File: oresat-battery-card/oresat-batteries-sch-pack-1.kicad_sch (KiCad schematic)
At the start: 92 parts, among them Q10 SI7111EDN-T1-GE3, Q13 SI7111EDN-T1-GE3, Q14 DMP2035UQ-7, Q15 DMP2035UQ-7, Q16 SI7111EDN-T1-GE3, Q17 SI7111EDN-T1-GE3, Q18 SI7111EDN-T1-GE3, Q19 SI7111EDN-T1-GE3, Q23 DMP2035UQ-7, Q29 SQS484ENW-T1_GE3, Q6 DMN2053UQ-13, Q7 DMN2053UQ-13, Q8 DMN2053UQ-13, Q9 DMN2053UQ-13, U10 TPS25983, U11 LTC4412, U12 MAX17205G, U8 S-8209AAA-T8T1U, U9 S-8209AAA-T8T1U

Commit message: Jumped back on the TPS bandwagon - LCSC to the rescue! - and lots of cleanup.
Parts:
- removed Q10: SI7111EDN-T1-GE3, Package_SO:Vishay_PowerPAK_1212-8_Single, symbol Transistor_FET:SiS443DN
- removed R69: 100k, oresat-passives:0603-C-NOSILK, symbol Device:R_Small_US
- added TP37, TP47: TEST-POINT-LARGE-SQUARE, oresat-misc:TestPoint-0.75mm-th, symbol oresat-misc:Test-Point-0.75mm-th
- C19: DPN 399-6856-1-ND -> (none); MPN C0603C104K5RACAUTO -> (none)
- JP1, JP2: now not fitted
- R107: value 100k -> 357K; DPN RMCF0603FT100KCT-ND -> RMCF0603FT357KCT-ND; MPN RMCF0603FT100K -> RMCF0603FT357K
- R45, R48, R52, R53: DPN RMCF0603FT2K70CT-ND -> RMCF0603FT1K00CT-ND
- R68: value 100k -> 2; DPN RMCF0603FT100KCT-ND -> RMCF0603FT2R00DKR-ND; MPN RMCF0603FT100K -> RMCF0603FT2R00
- R72: value 1870 -> 1k; DPN RMCF0603FT100KCT-ND -> RMCF0603FT1K00CT-ND; MPN RMCF0603FT100K -> RMCF0603FT1K00
- R74: value 210 -> 154; DPN RMCF0603FT100KCT-ND -> 738-RMCF0603FT154RCT-ND; MPN RMCF0603FT100K -> RMCF0603FT154R
- U10: value TPS25983 -> TPS259830ONRGER; DPN 296-TPS259830LNRGERCT-ND -> 296-TPS259830ONRGERCT-ND; MPN TPS25983 -> TPS259830ONRGER
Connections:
- net POS-BATT-DISC: now also R104.2, R107.1, U10.6 (EN/UVLO), TP47.1
- net VBUS: now also C10.1, C23.1, Q13.1 (S), Q13.2 (S), Q13.3 (S), Q18.5 (D), TP36.1, U11.1 (VIN)
- net at R72.1, U10.9 (IMON): now also TP37.1
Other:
- note added: "EFUSE Current limit: 8.0 A (circuit breaker set to +20%, 9.6 A) Voltage ramp up time: 24 ms Transient overcurrent timer: 2.0 ms Time between retries: 4.6 s"
- note added: "Q29 disconnects the - battery lead, but it also kills the ground reference for the ~{SHUTDOOWN} circuit, which is bad because it turns on the ABLIC and MAX17 chips. So, R93 preserves the ground reference while not allowing any appreciable current to flow."
- note removed: "EFUSE Current limit: 7.1 A Voltage ramp up time: 24 ms Transient overcurrent timer: 2.0 ms Time between retries: 4.6 s"
- note removed: "Q29 disconnects the - battery lead, but it also kills the ground reference for the ~{SHUTDOOWN} circuit, which is bad because it turns on the ABLIC and MAX17 chips. So, R93 preserves the ground reference while not allow anny appreciable current to flow."
- moved on the sheet: C10, Q29, R62, R85, R93, TP42, TP43

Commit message: Battery Card 4.0, no ERC or DRC errors or warnings
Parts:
- R107: value 357K -> 357k
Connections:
- net BATTNEG-PK1: no longer B2.2 (-), Q29.1 (S), Q29.2 (S), Q29.3 (S), R93.2, TP42.1
- new net: B2.2 (-), Q29.1 (S), Q29.2 (S), Q29.3 (S), R93.2, TP42.1
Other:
- note added: "TVS diode is next to main connector"
- moved on the sheet: C20, C21, C24, C25, D5, D6, JP1, JP2, Q14, Q15, Q16, Q17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

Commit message: Updated Makefile and Readme; fixed TCAN IC, cleanup, fix battery connections that were killed somehow
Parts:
- C19: DPN (none) -> 399-12984-1-ND; MPN (none) -> C0603C153K5RACAUTO
- R62: DPN 696-1374-1-ND -> WSLP-.01CT-ND; MFR Riedon -> Vishay Dale; MPN CSR1206-0R01F1 -> WSLP1206R0100FEA
- R68: DPN RMCF0603FT2R00DKR-ND -> RMCF0603FT2R00CT-ND
- U11: DPN MAX4211FETE+-ND -> LTC4412ES6#WTRMPBF; MPN MAX4211FETE -> LTC4412ES6#PBF
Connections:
- net BATTNEG-PK1: now also B2.2 (-), Q29.1 (S), Q29.2 (S), Q29.3 (S), R93.2, TP42.1
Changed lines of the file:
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@@
 	)
 	(junction
-		(at 365.76 294.64)
-		(diameter 0)
-		(color 0 0 0 0)
-	)
-	(junction
 		(at 365.76 270.51)
 		(diameter 0)
@@
 	)
 	(junction
+		(at 374.65 294.64)
+		(diameter 0)
+		(color 0 0 0 0)
+	)
+	(junction
 		(at 171.45 273.05)
 		(diameter 0)
@@
 	)
 	(junction
+		(at 365.76 294.64)
+		(diameter 0)
+		(color 0 0 0 0)
+	)
+	(junction
 		(at 327.66 82.55)
 		(diameter 0)
@@
 	)
 	(junction
+		(at 374.65 295.91)
+		(diameter 0)
+		(color 0 0 0 0)
+	)
+	(junction
 		(at 353.06 200.66)
 		(diameter 0)
@@
 	(wire
 		(pts
+			(xy 374.65 295.91) (xy 374.65 298.45)
+		)
+		(stroke
+			(width 0.381)
+			(type default)
+		)
+	)
+	(wire
+		(pts
 			(xy 231.14 163.83) (xy 231.14 172.72)
 		)
@@
 	(wire
 		(pts
-			(xy 365.76 294.64) (xy 422.91 294.64)
-		)
-		(stroke
-			(width 0.1524)
-			(type solid)
-		)
-	)
-	(wire
-		(pts
 			(xy 474.98 195.58) (xy 474.98 194.31)
 		)
@@
 	(wire
 		(pts
-			(xy 374.65 290.83) (xy 374.65 298.45)
+			(xy 374.65 290.83) (xy 374.65 294.64)
 		)
 		(stroke
@@
 	(wire
 		(pts
-			(xy 422.91 243.84) (xy 422.91 294.64)
+			(xy 422.91 243.84) (xy 422.91 295.91)
 		)
 		(stroke
@@
 	(wire
 		(pts
+			(xy 374.65 295.91) (xy 422.91 295.91)
+		)
+		(stroke
+			(width 0.1524)
+			(type solid)
+		)
+	)
+	(wire
+		(pts
 			(xy 485.14 195.58) (xy 485.14 194.31)
 		)
@@
 	(wire
 		(pts
+			(xy 365.76 294.64) (xy 374.65 294.64)
+		)
+		(stroke
+			(width 0.1524)
+			(type solid)
+		)
+	)
+	(wire
+		(pts
 			(xy 170.18 264.16) (xy 179.07 264.16)
 		)
@@
 	(wire
 		(pts
+			(xy 374.65 294.64) (xy 374.65 295.91)
+		)
+		(stroke
+			(width 0.381)
+			(type default)
+		)
+	)
+	(wire
+		(pts
 			(xy 374.65 71.12) (xy 374.65 72.39)
 		)
@@
 			)
 		)
-		(property "Datasheet" "https://search.kemet.com/download/specsheet/C0603C104K5RACAUTO"
+		(property "Datasheet" "https://yageogroup.com/content/datasheet/asset/file/KEM_C1023_X7R_AUTO_SMD"
 			(at 322.58 86.36 0)
 			(hide yes)
@@
 			)
 		)
-		(property "Description" ""
+		(property "Description" "0.015 µF ±10% 50V Ceramic Capacitor X7R 0603 (1608 Metric)"
 			(at 322.58 86.36 0)
 			(hide yes)
@@
 			)
 		)
-		(property "DPN" ""
+		(property "DPN" "399-12984-1-ND"
 			(at 322.58 86.36 0)
 			(hide yes)
@@
 			)
 		)
-		(property "MPN" ""
+		(property "MPN" "C0603C153K5RACAUTO"
 			(at 322.58 86.36 0)
 			(hide yes)
@@
 		)
 		(property "Value" "10n"
-			(at 249.174 188.976 0)
+			(at 249.174 188.468 0)
 			(show_name no)
 			(do_not_autoplace no)
@@
 			)
 		)
-		(property "DPN" "RMCF0603FT2R00DKR-ND"
+		(property "DPN" "RMCF0603FT2R00CT-ND"
 			(at 334.01 82.55 0)
 			(hide yes)
@@
 			)
 		)
-		(property "Datasheet" "https://www.mouser.com/datasheet/2/256/MAX4210-MAX4211-1265251.pdf"
+		(property "Datasheet" "https://www.analog.com/media/en/technical-documentation/data-sheets/ltc4412.pdf"
 			(at 377.19 99.06 0)
 			(hide yes)
@@
 			)
 		)
-		(property "Description" "Current Monitor Regulator High-Side 16-TQFN (4x4)"
+		(property "Description" "OR Controller Source Selector Switch P-Channel 2:1 TSOT-23-6 industrial temp"
 			(at 430.53 93.98 0)
 			(hide yes)
@@
 			)
 		)
-		(property "DPN" "MAX4211FETE+-ND"
+		(property "DPN" "LTC4412ES6#WTRMPBF"
 			(at 430.53 93.98 0)
 			(hide yes)
@@
 			)
 		)
-		(property "MPN" "MAX4211FETE"
+		(property "MPN" "LTC4412ES6#PBF"
 			(at 430.53 93.98 0)
 			(hide yes)
@@
 			)
 		)
-		(property "Datasheet" "https://riedon.com/media/pdf/CSR.pdf"
+		(property "Datasheet" "https://www.vishay.com/docs/30122/wslp.pdf"
 			(at 374.65 323.85 0)
 			(hide yes)
@@
 			)
 		)
-		(property "Description" "10 mOhms ±1% 1W Chip Resistor 1206 (3216 Metric) Current Sense, Non-Inductive Metal Element"
+		(property "Description" "10 mOhms ±1% 1W Chip Resistor 1206 (3216 Metric) Anti-Sulfur, Automotive AEC-Q200, Current Sense, Moisture Resistant, Pulse Withstanding Metal Element"
 			(at 374.65 323.85 0)
 			(hide yes)
@@
 			)
 		)
-		(property "DPN" "696-1374-1-ND"
+		(property "DPN" "WSLP-.01CT-ND"
 			(at 374.65 323.85 0)
 			(hide yes)
@@
 			)
 		)
-		(property "MFR" "Riedon"
+		(property "MFR" "Vishay Dale"
 			(at 374.65 323.85 0)
 			(hide yes)
@@
 			)
 		)
-		(property "MPN" "CSR1206-0R01F1"
+		(property "MPN" "WSLP1206R0100FEA"
 			(at 374.65 323.85 0)
 			(hide yes)
@@
 		(lib_id "Device:C_Small")
 		(at 231.14 175.26 0)
+		(mirror y)
 		(unit 1)
 		(body_style 1)
@@
 		(dnp no)
 		(property "Reference" "C17"
-			(at 233.426 174.752 0)
+			(at 228.854 174.752 0)
 			(show_name no)
 			(do_not_autoplace no)
@@
 		)
 		(property "Value" "100n"
-			(at 233.68 176.784 0)
+			(at 228.6 176.784 0)
 			(show_name no)
 			(do_not_autoplace no)

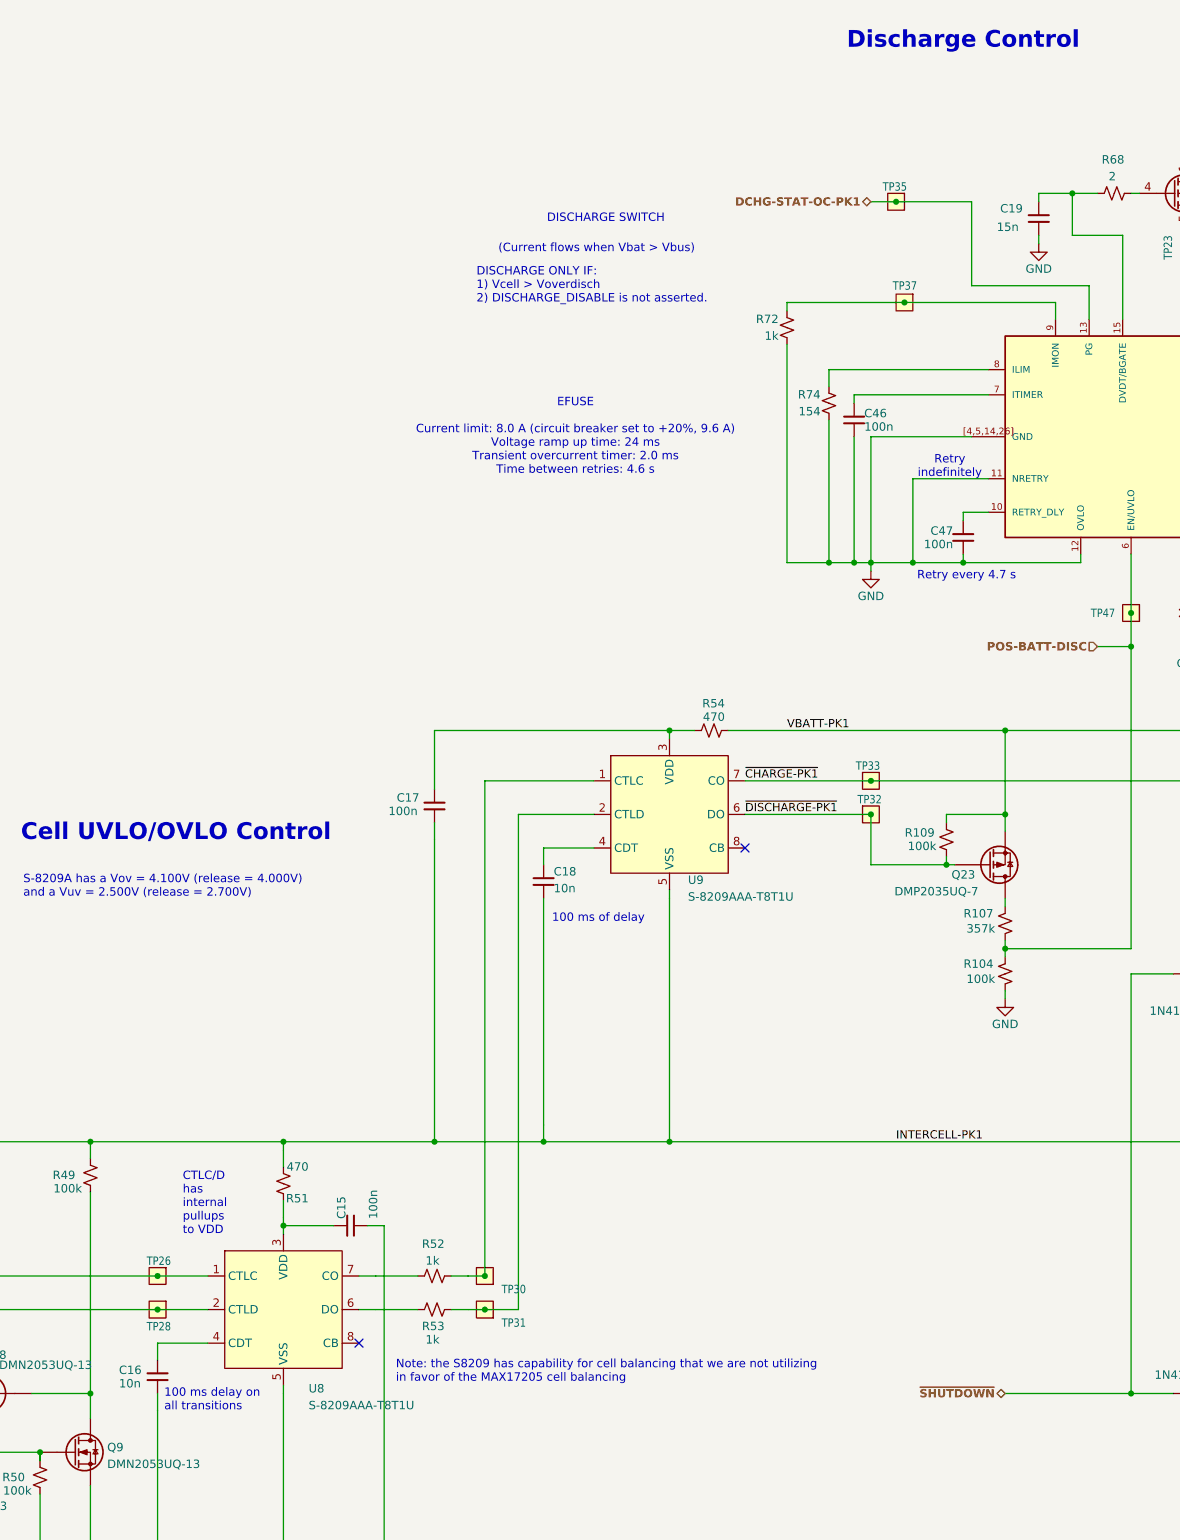
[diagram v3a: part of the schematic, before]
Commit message: Changes to eFuse after trying evaluation board, and recalculating values, and trying to reduce number of passive components to minimum number
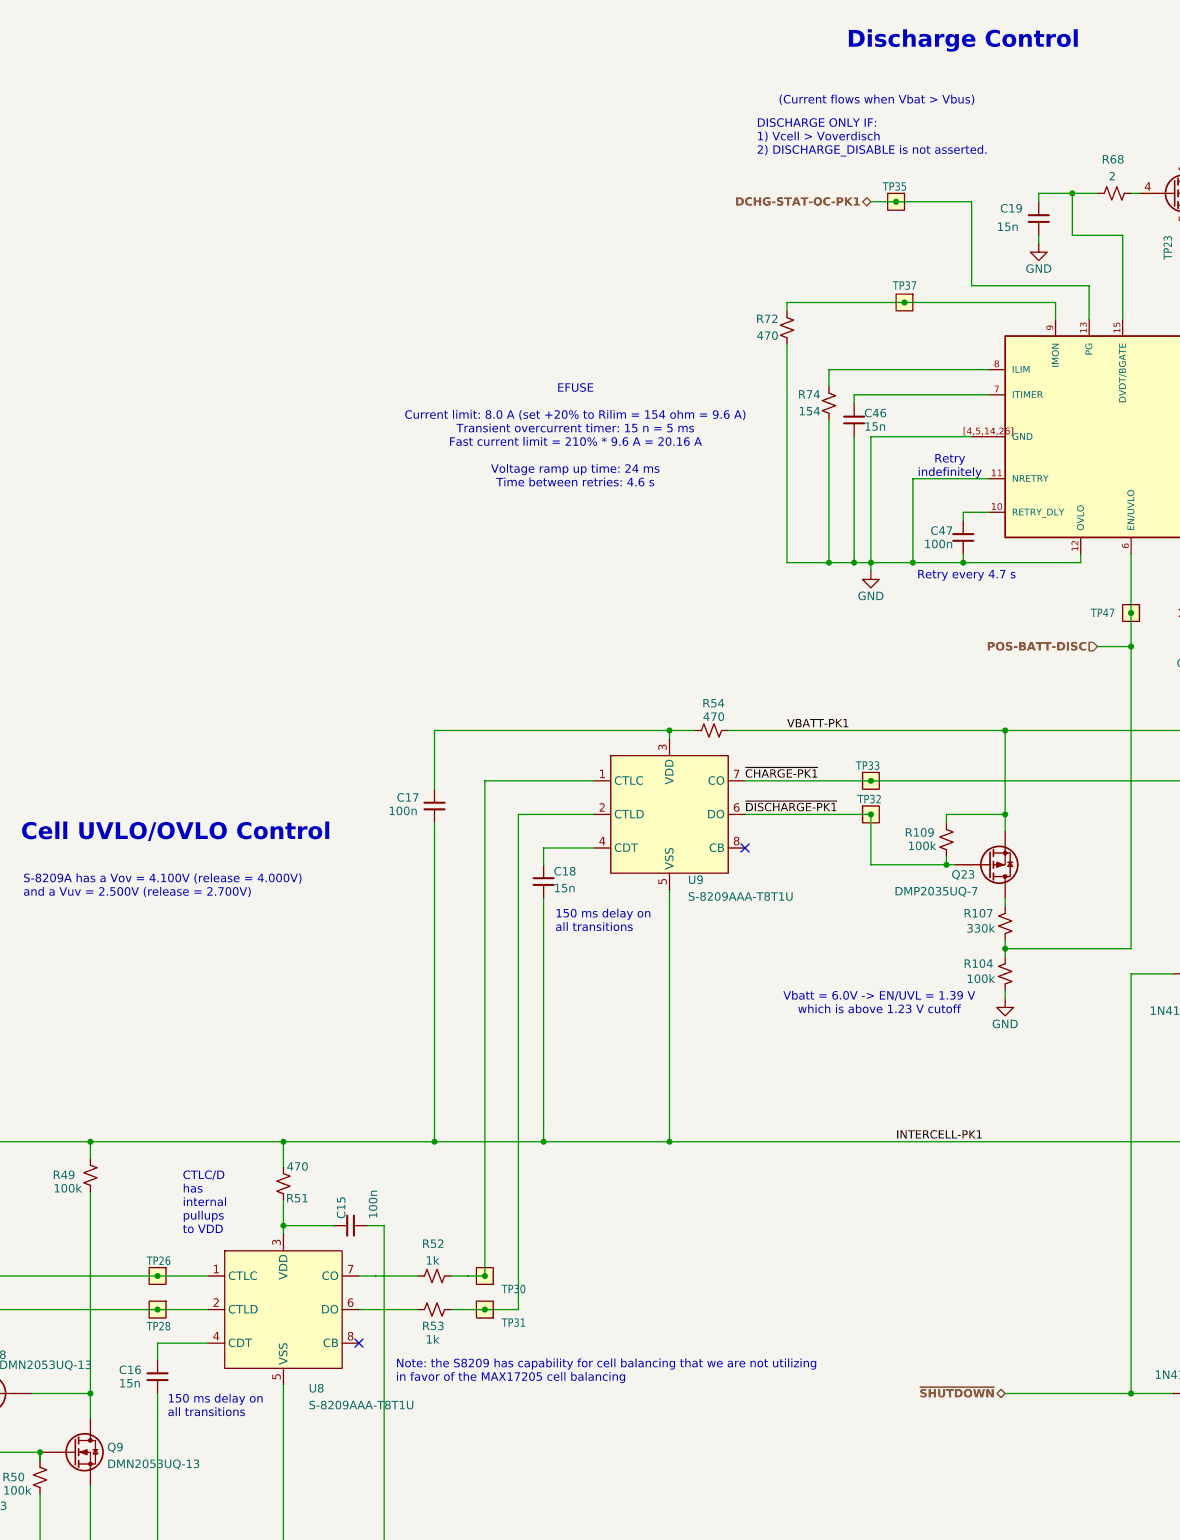
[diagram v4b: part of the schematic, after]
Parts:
- C16, C18: value 10n -> 15n; DPN 399-12983-1-ND -> 399-12984-1-ND; MPN C0603C103J5RACAUTO -> C0603C153K5RACAUTO
- C46: value 100n -> 15n; DPN 399-6856-1-ND -> 399-12984-1-ND; MPN C0603C104K5RACAUTO -> C0603C153K5RACAUTO
- R107: value 357k -> 330k; DPN RMCF0603FT357KCT-ND -> RMCF0603FT330KCT-ND; MPN RMCF0603FT357K -> RMCF0603FT330K
- R72: value 1k -> 470; DPN RMCF0603FT1K00CT-ND -> RMCF0603FT470RCT-ND; MPN RMCF0603FT1K00 -> RMCF0603FT470R
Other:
- note added: "150 ms delay on all transitions"
- note added: "EFUSE Current limit: 8.0 A (set +20% to Rilim = 154 ohm = 9.6 A) Transient overcurrent timer: 15 n = 5 ms Fast current limit = 210% * 9.6 A = 20.16 A Voltage ramp up time: 24 ms Time between retries: 4.6 s"
- note added: "Vbatt = 6.0V -> EN/UVL = 1.39 V which is above 1.23 V cutoff"
- note removed: "100 ms delay on all transitions"
- note removed: "100 ms of delay"
- note removed: "DISCHARGE SWITCH"
- note removed: "EFUSE Current limit: 8.0 A (circuit breaker set to +20%, 9.6 A) Voltage ramp up time: 24 ms Transient overcurrent timer: 2.0 ms Time between retries: 4.6 s"
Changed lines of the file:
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@@
 		)
 	)
+	(text "150 ms delay on\nall transitions"
+		(exclude_from_sim no)
+		(at 190.754 267.97 0)
+		(effects
+			(font
+				(size 1.27 1.27)
+			)
+			(justify left bottom)
+		)
+	)
 	(text "CTLC/D\nhas\ninternal\npullups\nto VDD"
 		(exclude_from_sim no)
@@
 		)
 	)
-	(text "EFUSE\n\nCurrent limit: 8.0 A (circuit breaker set to +20%, 9.6 A)\nVoltage ramp up time: 24 ms\nTransient overcurrent timer: 2.0 ms\nTime between retries: 4.6 s"
+	(text "EFUSE\n\nCurrent limit: 8.0 A (set +20% to Rilim = 154 ohm = 9.6 A)\nTransient overcurrent timer: 15 n = 5 ms\nFast current limit = 210% * 9.6 A = 20.16 A\n\nVoltage ramp up time: 24 ms\nTime between retries: 4.6 s"
 		(exclude_from_sim no)
 		(at 252.476 119.38 0)
@@
 		)
 	)
+	(text "Vbatt = 6.0V -> EN/UVL = 1.39 V\nwhich is above 1.23 V cutoff"
+		(exclude_from_sim no)
+		(at 298.45 205.232 0)
+		(effects
+			(font
+				(size 1.27 1.27)
+			)
+		)
+	)
 	(text "(Current flows when Vbat > Vbus)"
 		(exclude_from_sim no)
-		(at 240.792 91.694 0)
+		(at 283.21 69.342 0)
+		(effects
+			(font
+				(size 1.27 1.27)
+			)
+			(justify left bottom)
+		)
+	)
+	(text "150 ms delay on\nall transitions"
+		(exclude_from_sim no)
+		(at 249.428 194.564 0)
 		(effects
 			(font
@@
 		)
 	)
-	(text "DISCHARGE SWITCH"
-		(exclude_from_sim no)
-		(at 248.158 87.122 0)
-		(effects
-			(font
-				(size 1.27 1.27)
-			)
-			(justify left bottom)
-		)
-	)
 	(text "Referenced to B2- (top of shunt), not system\nGND which is bottom of shunt."
 		(exclude_from_sim no)
@@
 		)
 	)
-	(text "100 ms delay on\nall transitions"
-		(exclude_from_sim no)
-		(at 190.246 266.954 0)
-		(effects
-			(font
-				(size 1.27 1.27)
-			)
-			(justify left bottom)
-		)
-	)
 	(text "2x Honeywell 197-103LAG-A01"
 		(exclude_from_sim no)
@@
 	(text "DISCHARGE ONLY IF:\n1) Vcell > Voverdisch\n2) DISCHARGE_DISABLE is not asserted."
 		(exclude_from_sim no)
-		(at 237.49 99.314 0)
-		(effects
-			(font
-				(size 1.27 1.27)
-			)
-			(justify left bottom)
-		)
-	)
-	(text "100 ms of delay"
-		(exclude_from_sim no)
-		(at 248.92 193.04 0)
+		(at 279.908 76.962 0)
 		(effects
 			(font
@@
 			)
 		)
-		(property "Value" "10n"
+		(property "Value" "15n"
 			(at 183.388 263.398 0)
 			(show_name no)
@@
 			)
 		)
-		(property "Datasheet" "https://www.yageogroup.com/content/datasheet/asset/file/KEM_C1023_X7R_AUTO_SMD"
+		(property "Datasheet" "https://yageogroup.com/content/datasheet/asset/file/KEM_C1023_X7R_AUTO_SMD"
 			(at 189.23 261.62 0)
 			(hide yes)
@@
 			)
 		)
-		(property "Description" "10000 pF ±5% 50V Ceramic Capacitor X7R 0603 (1608 Metric)"
+		(property "Description" "0.015 µF ±10% 50V Ceramic Capacitor X7R 0603 (1608 Metric)"
 			(at 189.23 261.62 0)
 			(hide yes)
@@
 			)
 		)
-		(property "DPN" "399-12983-1-ND"
+		(property "DPN" "399-12984-1-ND"
 			(at 189.23 261.62 0)
 			(hide yes)
@@
 			)
 		)
-		(property "MPN" "C0603C103J5RACAUTO"
+		(property "MPN" "C0603C153K5RACAUTO"
 			(at 189.23 261.62 0)
 			(hide yes)
@@
 			)
 		)
-		(property "Value" "10n"
+		(property "Value" "15n"
 			(at 249.174 188.468 0)
 			(show_name no)
@@
 			)
 		)
-		(property "Datasheet" "https://www.yageogroup.com/content/datasheet/asset/file/KEM_C1023_X7R_AUTO_SMD"
+		(property "Datasheet" "https://yageogroup.com/content/datasheet/asset/file/KEM_C1023_X7R_AUTO_SMD"
 			(at 247.65 186.69 0)
 			(hide yes)
@@
 			)
 		)
-		(property "Description" "10000 pF ±5% 50V Ceramic Capacitor X7R 0603 (1608 Metric)"
+		(property "Description" "0.015 µF ±10% 50V Ceramic Capacitor X7R 0603 (1608 Metric)"
 			(at 247.65 186.69 0)
 			(hide yes)
@@
 			)
 		)
-		(property "DPN" "399-12983-1-ND"
+		(property "DPN" "399-12984-1-ND"
 			(at 247.65 186.69 0)
 			(hide yes)
@@
 			)
 		)
-		(property "MPN" "C0603C103J5RACAUTO"
+		(property "MPN" "C0603C153K5RACAUTO"
 			(at 247.65 186.69 0)
 			(hide yes)
@@
 			)
 		)
-		(property "Value" "357k"
+		(property "Value" "330k"
 			(at 315.976 194.564 0)
 			(show_name no)
@@
 			)
 		)
-		(property "Description" "357 kOhms ±1% 0.1W, 1/10W Chip Resistor 0603 (1608 Metric) Automotive AEC-Q200 Thick Film"
+		(property "Description" "330 kOhms ±1% 0.1W, 1/10W Chip Resistor 0603 (1608 Metric) Automotive AEC-Q200 Thick Film"
 			(at 317.5 193.04 0)
 			(hide yes)
@@
 			)
 		)
-		(property "DPN" "RMCF0603FT357KCT-ND"
+		(property "DPN" "RMCF0603FT330KCT-ND"
 			(at 317.5 193.04 0)
 			(hide yes)
@@
 			)
 		)
-		(property "MPN" "RMCF0603FT357K"
+		(property "MPN" "RMCF0603FT330K"
 			(at 317.5 193.04 0)
 			(hide yes)
@@
 			)
 		)
-		(property "Value" "100n"
+		(property "Value" "15n"
 			(at 296.164 118.618 0)
 			(show_name no)
@@
 			)
 		)
-		(property "Datasheet" "https://search.kemet.com/download/specsheet/C0603C104K5RACAUTO"
+		(property "Datasheet" "https://yageogroup.com/content/datasheet/asset/file/KEM_C1023_X7R_AUTO_SMD"
 			(at 294.64 116.84 0)
 			(hide yes)
@@
 			)
 		)
-		(property "Description" "0.1 µF ±10% 50V Ceramic Capacitor X7R 0603 (1608 Metric)"
+		(property "Description" "0.015 µF ±10% 50V Ceramic Capacitor X7R 0603 (1608 Metric)"
 			(at 294.64 116.84 0)
 			(hide yes)
@@
 			)
 		)
-		(property "DPN" "399-6856-1-ND"
+		(property "DPN" "399-12984-1-ND"
 			(at 294.64 116.84 0)
 			(hide yes)
@@
 			)
 		)
-		(property "MPN" "C0603C104K5RACAUTO"
+		(property "MPN" "C0603C153K5RACAUTO"
 			(at 294.64 116.84 0)
 			(hide yes)
@@
 			)
 		)
-		(property "Value" "1k"
+		(property "Value" "470"
 			(at 283.21 103.378 0)
 			(show_name no)
@@
 			)
 		)
-		(property "Description" "1 kOhms ±1% 0.1W, 1/10W Chip Resistor 0603 (1608 Metric) Automotive AEC-Q200 Thick Film"
+		(property "Description" "470 Ohms ±1% 0.1W, 1/10W Chip Resistor 0603 (1608 Metric) Automotive AEC-Q200 Thick Film"
 			(at 284.48 102.87 0)
 			(hide yes)
@@
 			)
 		)
-		(property "DPN" "RMCF0603FT1K00CT-ND"
+		(property "DPN" "RMCF0603FT470RCT-ND"
 			(at 284.48 102.87 0)
 			(hide yes)
@@
 			)
 		)
-		(property "MPN" "RMCF0603FT1K00"
+		(property "MPN" "RMCF0603FT470R"
 			(at 284.48 102.87 0)
 			(hide yes)
